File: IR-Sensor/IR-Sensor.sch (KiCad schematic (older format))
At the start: 9 parts

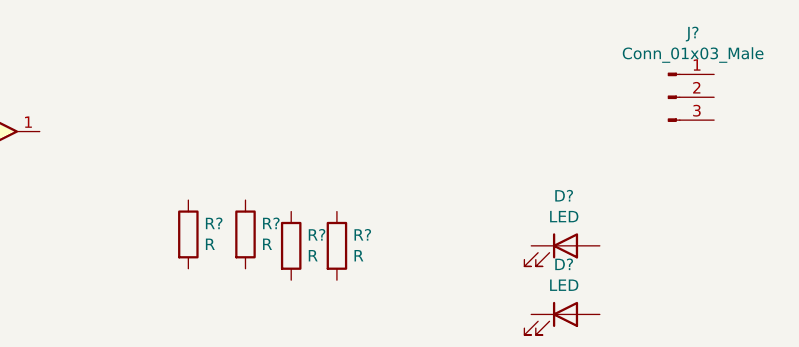
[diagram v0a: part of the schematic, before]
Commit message: Added Photodiode
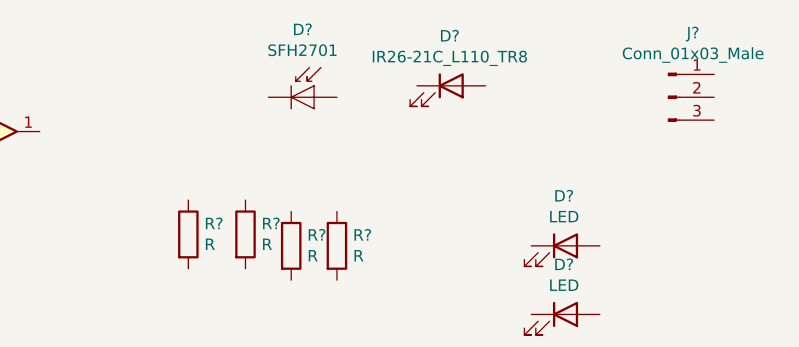
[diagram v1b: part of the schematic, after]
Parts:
- added D?: SFH2701, LED_SMD:LED_1206_3216Metric_Castellated, symbol Sensor_Optical:SFH2701
- added D?: IR26-21C_L110_TR8, LED_SMD:LED_1206_3216Metric, symbol LED:IR26-21C_L110_TR8
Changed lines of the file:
@@
+	1    0    0    -1
+$EndComp
+$Comp
+L Sensor_Optical:SFH2701 D?
+U 1 1 5FF3F560
+P 3250 1200
+F 0 "D?" H 3200 1495 50  0000 C CNN
+F 1 "SFH2701" H 3200 1404 50  0000 C CNN
+F 2 "LED_SMD:LED_1206_3216Metric_Castellated" H 3250 1375 50  0001 C CNN
+F 3 "http://www.osram-os.com/Graphics/XPic6/00201111_0.pdf/SFH%202701.pdf" H 3200 1200 50  0001 C CNN
+	1    3250 1200
+	1    0    0    -1
+$EndComp
+$Comp
+L LED:IR26-21C_L110_TR8 D?
+U 1 1 5FF3FBB9
+P 3850 1150
+F 0 "D?" H 3843 1367 50  0000 C CNN
+F 1 "IR26-21C_L110_TR8" H 3843 1276 50  0000 C CNN
+F 2 "LED_SMD:LED_1206_3216Metric" H 3850 1350 50  0001 C CNN
+F 3 "http://www.everlight.com/file/ProductFile/IR26-21C-L110-TR8.pdf" H 3850 1150 50  0001 C CNN
+	1    3850 1150
 	1    0    0    -1
 $EndComp

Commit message: Added footprint & netlist
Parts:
- removed D?: LED, symbol Device:LED
- removed R?: R, symbol Device:R
- added D3: LED, LED_SMD:LED_0805_2012Metric, symbol Device:LED
- added R3: R, Resistor_SMD:R_0805_2012Metric, symbol Device:R
- D4: renamed from D?; footprint (none) -> LED_SMD:LED_0805_2012Metric
- J1: renamed from J?; footprint (none) -> Connector_PinHeader_2.54mm:PinHeader_1x03_P2.54mm_Horizontal
- R1, R2, R4: renamed from R?; footprint (none) -> Resistor_SMD:R_0805_2012Metric
- RV1: renamed from RV?; footprint (none) -> Potentiometer_SMD:Potentiometer_Bourns_3314J_Vertical
- U1: renamed from U?; footprint (none) -> Package_SO:TSSOP-14_4.4x5mm_P0.65mm
- gave numbers to parts that had none: 2
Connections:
- net GND: now reaches D4.1 (K)
- net GND: now also D1.1 (K), D2.1 (K), J1.1 (Pin_1), RV1.3, D3.1 (K)
- net at D4.2 (A): now also R4.2
- net VCC: now reaches R2.1
- net VCC: now also J1.3 (Pin_3), R1.1, R4.1, RV1.1
- net at R2.2: now also D2.2 (A), U1.3 (+)
- net at R1.2: now also D1.2 (A)
- net OUTPUT: now reaches U1.1
- net OUTPUT: now also J1.2 (Pin_2), R3.1
- net at U1.2 (-): now also RV1.2
- new net: D3.2 (A), R3.2
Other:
- note added: "CONNECTOR"
- note added: "IC CONNECTION"
- note added: "LED INDICATOR"
- moved on the sheet: D1, D2, D4, J1, R1, R2, R4, RV1, U1A

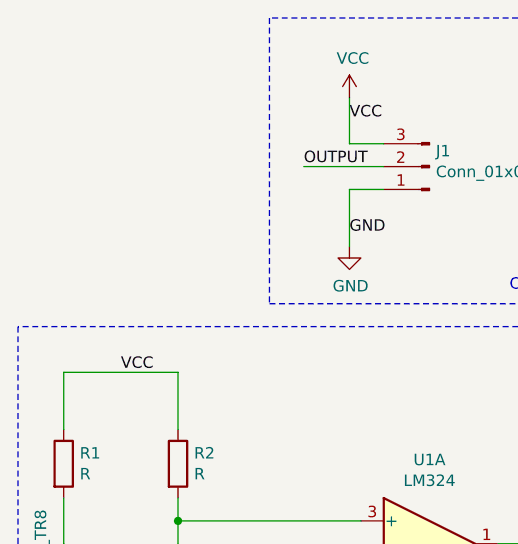
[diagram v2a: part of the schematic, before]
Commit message: Added reference max voltage
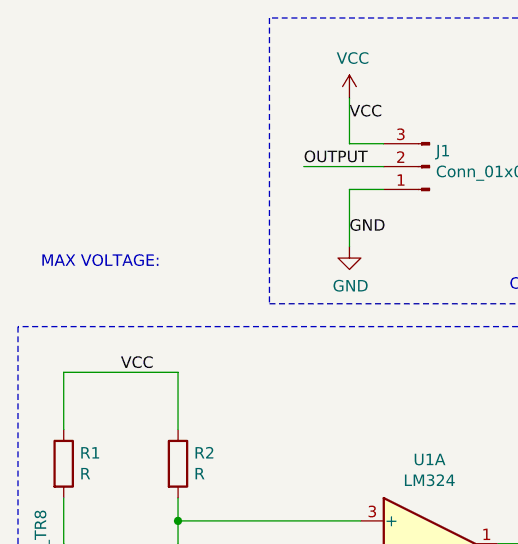
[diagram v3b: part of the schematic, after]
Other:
- note added: "MAX VOLTAGE:"
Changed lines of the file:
@@
 Wire Notes Line
 	6750 3350 6750 4850
+Text Notes 4100 3100 0    50   ~ 0
+MAX VOLTAGE:
 $EndSCHEMATC

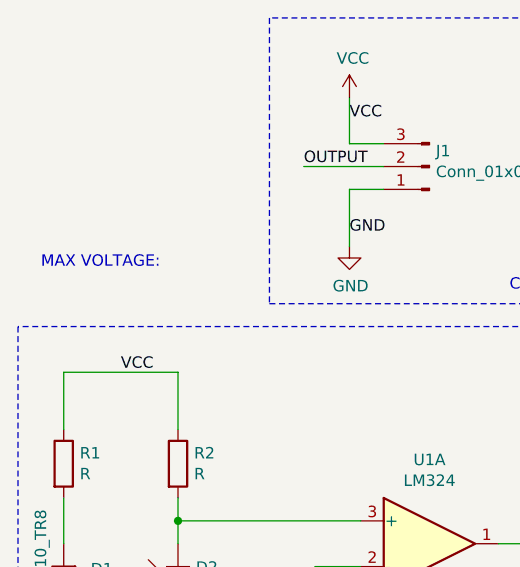
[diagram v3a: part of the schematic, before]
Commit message: Added reference max current
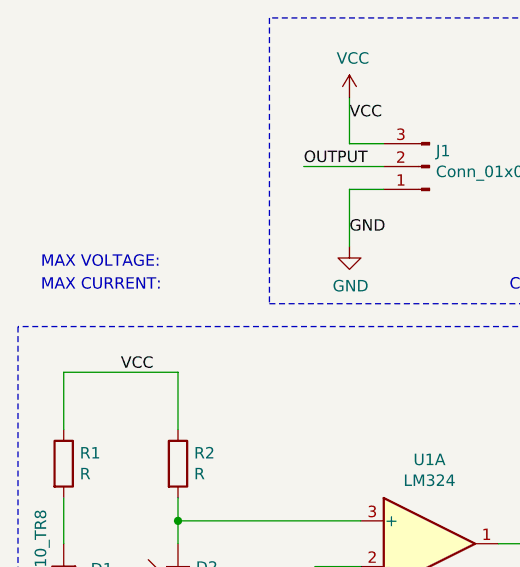
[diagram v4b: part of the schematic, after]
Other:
- note added: "MAX CURRENT:"
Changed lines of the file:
@@
 Text Notes 4100 3100 0    50   ~ 0
 MAX VOLTAGE:
+Text Notes 4100 3200 0    50   ~ 0
+MAX CURRENT:
 $EndSCHEMATC

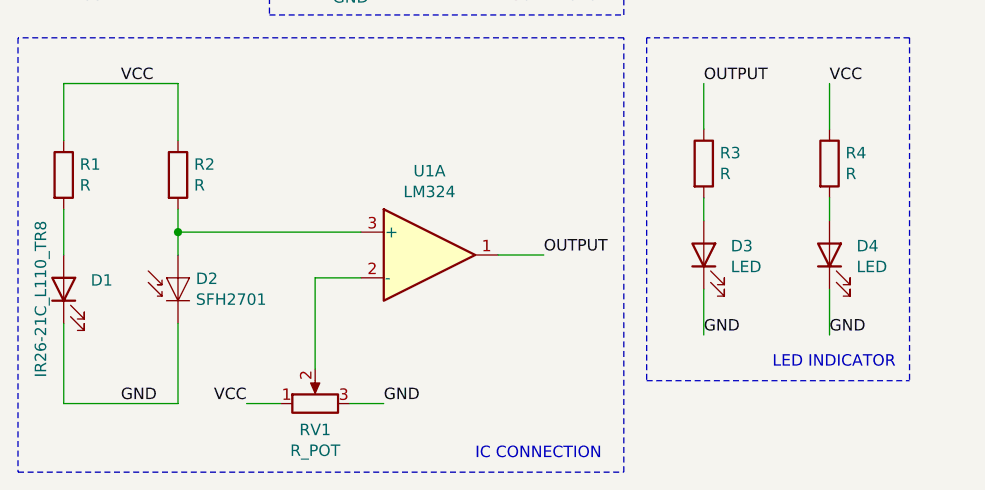
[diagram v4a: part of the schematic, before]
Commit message: Added value of resistor
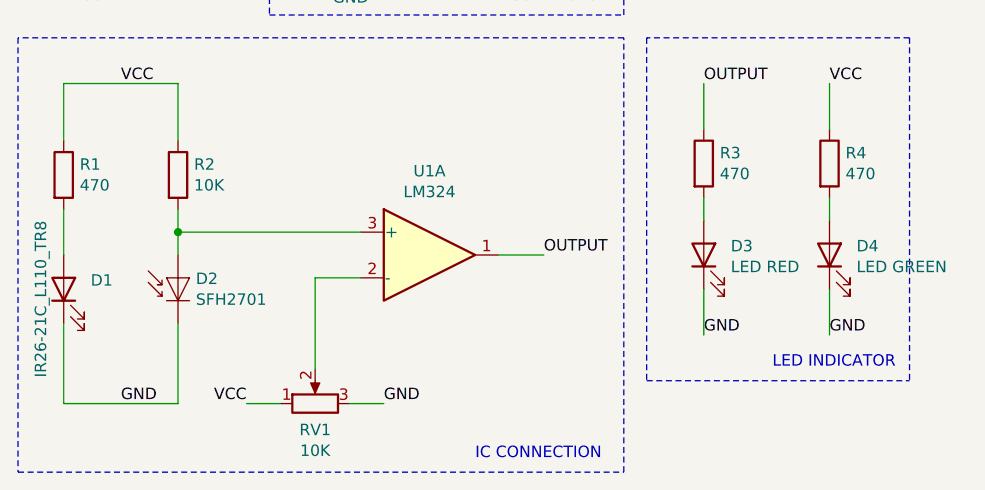
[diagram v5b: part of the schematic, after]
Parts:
- D3: value LED -> LED RED
- D4: value LED -> LED GREEN
- R1, R3, R4: value R -> 470
- R2: value R -> 10K
- RV1: value R_POT -> 10K
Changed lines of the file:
@@
 P 7550 4300
 F 0 "D4" V 7589 4182 50  0000 R CNN
-F 1 "LED" V 7498 4182 50  0000 R CNN
+F 1 "LED GREEN" V 7498 4182 50  0000 R CNN
 F 2 "LED_SMD:LED_0805_2012Metric" H 7550 4300 50  0001 C CNN
 F 3 "~" H 7550 4300 50  0001 C CNN
@@
 P 4700 3950
 F 0 "R2" H 4770 3996 50  0000 L CNN
-F 1 "R" H 4770 3905 50  0000 L CNN
+F 1 "10K" H 4770 3905 50  0000 L CNN
 F 2 "Resistor_SMD:R_0805_2012Metric" V 4630 3950 50  0001 C CNN
 F 3 "~" H 4700 3950 50  0001 C CNN
@@
 P 7550 3900
 F 0 "R4" H 7620 3946 50  0000 L CNN
-F 1 "R" H 7620 3855 50  0000 L CNN
+F 1 "470" H 7620 3855 50  0000 L CNN
 F 2 "Resistor_SMD:R_0805_2012Metric" V 7480 3900 50  0001 C CNN
 F 3 "~" H 7550 3900 50  0001 C CNN
@@
 P 4200 3950
 F 0 "R1" H 4270 3996 50  0000 L CNN
-F 1 "R" H 4270 3905 50  0000 L CNN
+F 1 "470" H 4270 3905 50  0000 L CNN
 F 2 "Resistor_SMD:R_0805_2012Metric" V 4130 3950 50  0001 C CNN
 F 3 "~" H 4200 3950 50  0001 C CNN
@@
 P 5300 4950
 F 0 "RV1" V 5185 4950 50  0000 C CNN
-F 1 "R_POT" V 5094 4950 50  0000 C CNN
+F 1 "10K" V 5094 4950 50  0000 C CNN
 F 2 "Potentiometer_SMD:Potentiometer_Bourns_3314J_Vertical" H 5300 4950 50  0001 C CNN
 F 3 "~" H 5300 4950 50  0001 C CNN
@@
 P 7000 4300
 F 0 "D3" V 7039 4182 50  0000 R CNN
-F 1 "LED" V 6948 4182 50  0000 R CNN
+F 1 "LED RED" V 6948 4182 50  0000 R CNN
 F 2 "LED_SMD:LED_0805_2012Metric" H 7000 4300 50  0001 C CNN
 F 3 "~" H 7000 4300 50  0001 C CNN
@@
 P 7000 3900
 F 0 "R3" H 7070 3946 50  0000 L CNN
-F 1 "R" H 7070 3855 50  0000 L CNN
+F 1 "470" H 7070 3855 50  0000 L CNN
 F 2 "Resistor_SMD:R_0805_2012Metric" V 6930 3900 50  0001 C CNN
 F 3 "~" H 7000 3900 50  0001 C CNN

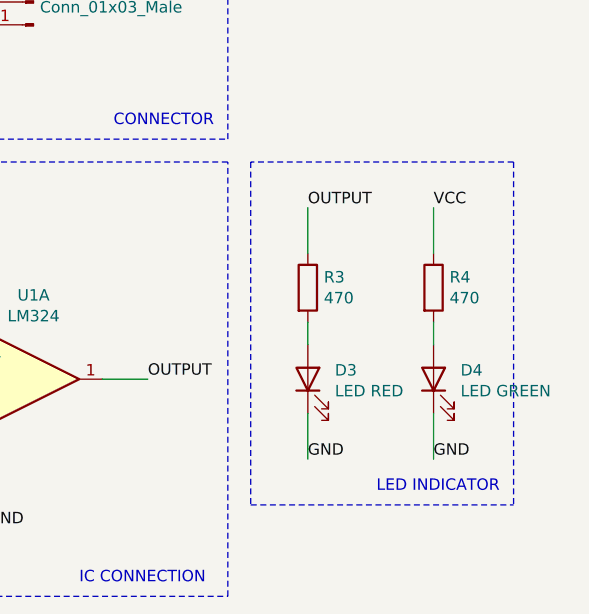
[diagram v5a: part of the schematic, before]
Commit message: Added text skillscreen
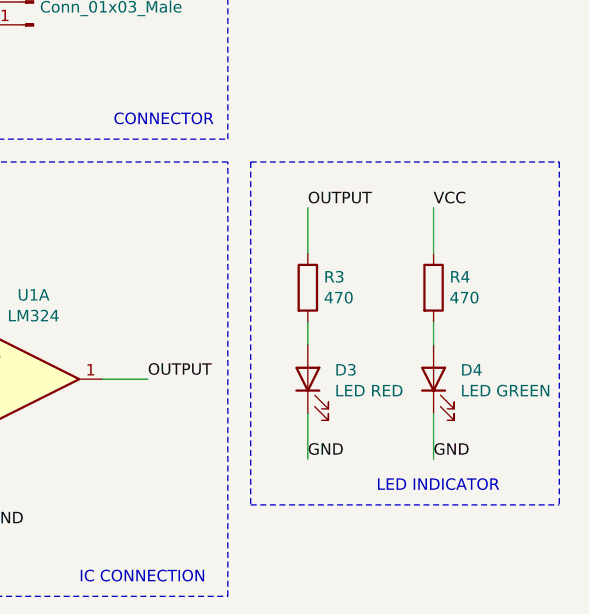
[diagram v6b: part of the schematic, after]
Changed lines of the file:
@@
 Wire Notes Line
 	6650 2000 5100 2000
-Wire Notes Line
-	6750 4850 7900 4850
-Wire Notes Line
-	7900 3350 6750 3350
 Text Notes 6000 5200 0    50   ~ 0
 IC CONNECTION
@@
 LED INDICATOR
 Wire Notes Line
-	7900 3350 7900 4850
+	8100 3350 8100 4850
 Wire Notes Line
 	6750 3350 6750 4850
@@
 Text Notes 4100 3200 0    50   ~ 0
 MAX CURRENT:
+Wire Notes Line
+	6750 4850 8100 4850
+Wire Notes Line
+	6750 3350 8100 3350
 $EndSCHEMATC
